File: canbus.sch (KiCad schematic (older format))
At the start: 17 parts, among them J1 Conn_01x08, J2 RJ45, J3 RJ45, U1 MCP2515-E/SO, U2 MCP2562-H/SN, Y1 Crystal_GND24

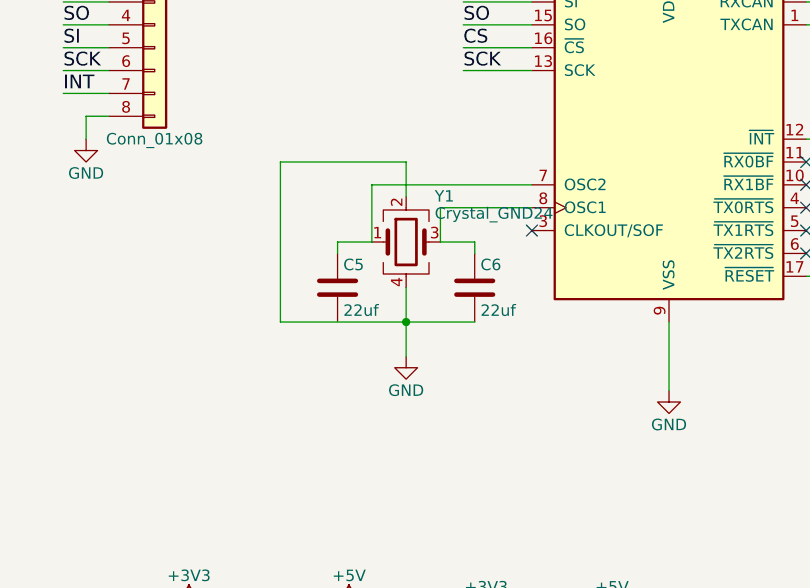
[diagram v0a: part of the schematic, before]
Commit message: Modified layout to include capacitors for oscillator
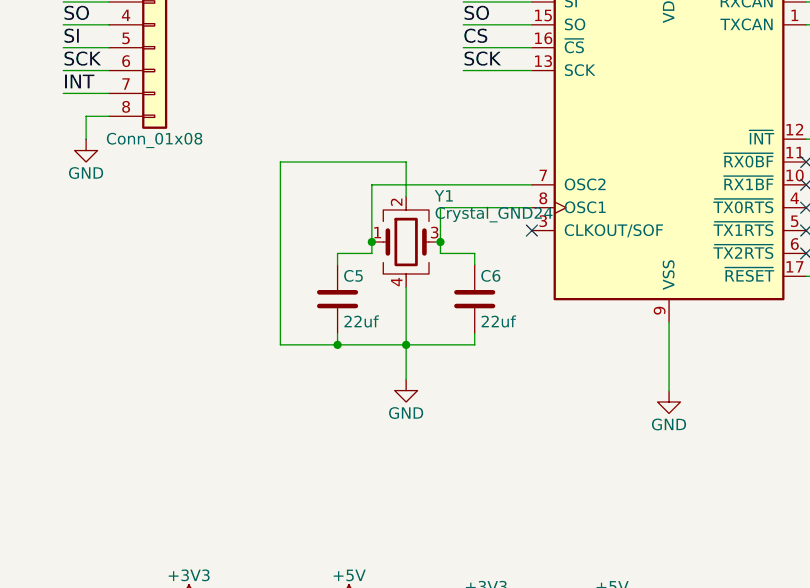
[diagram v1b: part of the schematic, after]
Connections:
- net GND: now also C5.2
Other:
- moved on the sheet: C5, C6
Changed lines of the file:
@@
 L GND #PWR05
 U 1 1 59E47374
-P 3300 4100
-F 0 "#PWR05" H 3300 3850 50  0001 C CNN
-F 1 "GND" H 3300 3950 50  0000 C CNN
-F 2 "" H 3300 4100 50  0001 C CNN
-F 3 "" H 3300 4100 50  0001 C CNN
-	1    3300 4100
+P 3300 4200
+F 0 "#PWR05" H 3300 3950 50  0001 C CNN
+F 1 "GND" H 3300 4050 50  0000 C CNN
+F 2 "" H 3300 4200 50  0001 C CNN
+F 3 "" H 3300 4200 50  0001 C CNN
+	1    3300 4200
 	1    0    0    -1
 $EndComp
@@
 	6200 2300 6200 2600
 Wire Wire Line
-	3450 3600 3450 3450
+	3450 3450 3450 3650
 Wire Wire Line
 	3450 3450 3850 3450
 Wire Wire Line
-	3150 3600 3150 3350
-Wire Wire Line
-	3150 3350 3850 3350
-Wire Wire Line
-	3300 3800 3300 4100
+	3150 3350 3150 3650
+Wire Wire Line
+	3300 3800 3300 4200
 Wire Wire Line
 	5050 3750 5150 3750
@@
 	3300 3250 2750 3250
 Wire Wire Line
-	2750 3250 2750 3950
-Wire Wire Line
-	2750 3950 3600 3950
-Connection ~ 3300 3950
+	2750 3250 2750 4050
+Wire Wire Line
+	2750 4050 3600 4050
+Connection ~ 3300 4050
 Wire Wire Line
 	8900 1950 8900 2000
@@
 L C C5
 U 1 1 5B05E18A
-P 3000 3800
-F 0 "C5" H 3025 3900 50  0000 L CNN
-F 1 "22uf" H 3025 3700 50  0000 L CNN
-F 2 "Capacitors_SMD:C_0805_HandSoldering" H 3038 3650 50  0001 C CNN
-F 3 "" H 3000 3800 50  0001 C CNN
-	1    3000 3800
+P 3000 3850
+F 0 "C5" H 3025 3950 50  0000 L CNN
+F 1 "22uf" H 3025 3750 50  0000 L CNN
+F 2 "Capacitors_SMD:C_0805_HandSoldering" H 3038 3700 50  0001 C CNN
+F 3 "" H 3000 3850 50  0001 C CNN
+	1    3000 3850
 	1    0    0    -1
 $EndComp
@@
 L C C6
 U 1 1 5B05E20B
-P 3600 3800
-F 0 "C6" H 3625 3900 50  0000 L CNN
-F 1 "22uf" H 3625 3700 50  0000 L CNN
-F 2 "Capacitors_SMD:C_0805_HandSoldering" H 3638 3650 50  0001 C CNN
-F 3 "" H 3600 3800 50  0001 C CNN
-	1    3600 3800
-	1    0    0    -1
-$EndComp
-Wire Wire Line
-	3000 3650 3000 3600
-Wire Wire Line
-	3000 3600 3150 3600
-Wire Wire Line
-	3450 3600 3600 3600
-Wire Wire Line
-	3600 3600 3600 3650
+P 3600 3850
+F 0 "C6" H 3625 3950 50  0000 L CNN
+F 1 "22uf" H 3625 3750 50  0000 L CNN
+F 2 "Capacitors_SMD:C_0805_HandSoldering" H 3638 3700 50  0001 C CNN
+F 3 "" H 3600 3850 50  0001 C CNN
+	1    3600 3850
+	1    0    0    -1
+$EndComp
+Wire Wire Line
+	3000 4000 3000 4050
+Connection ~ 3000 4050
+Wire Wire Line
+	3600 4050 3600 4000
+Wire Wire Line
+	3150 3350 3850 3350
+Wire Wire Line
+	3000 3700 3000 3650
+Wire Wire Line
+	3000 3650 3150 3650
+Connection ~ 3150 3600
+Wire Wire Line
+	3450 3650 3600 3650
+Wire Wire Line
+	3600 3650 3600 3700
+Connection ~ 3450 3600
 $EndSCHEMATC

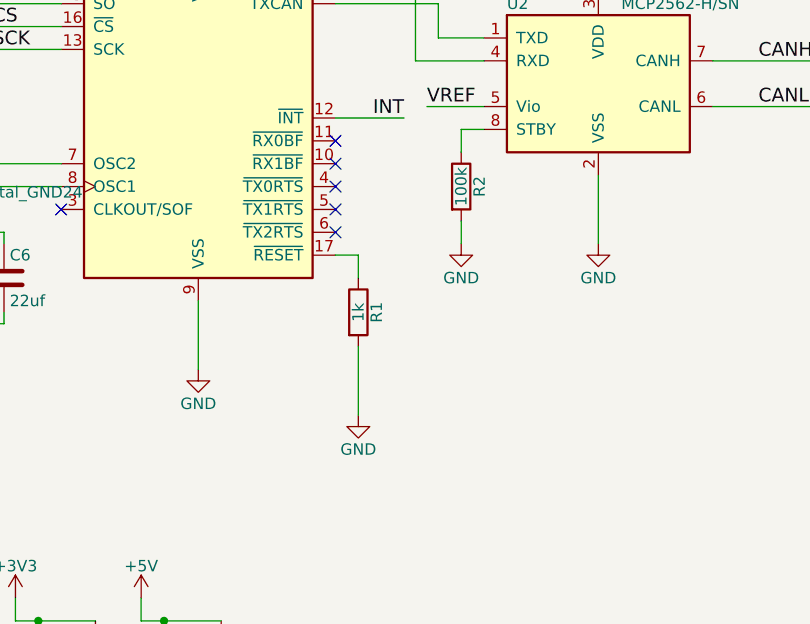
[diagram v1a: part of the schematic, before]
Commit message: Fixed MCP2515 Reset pullup
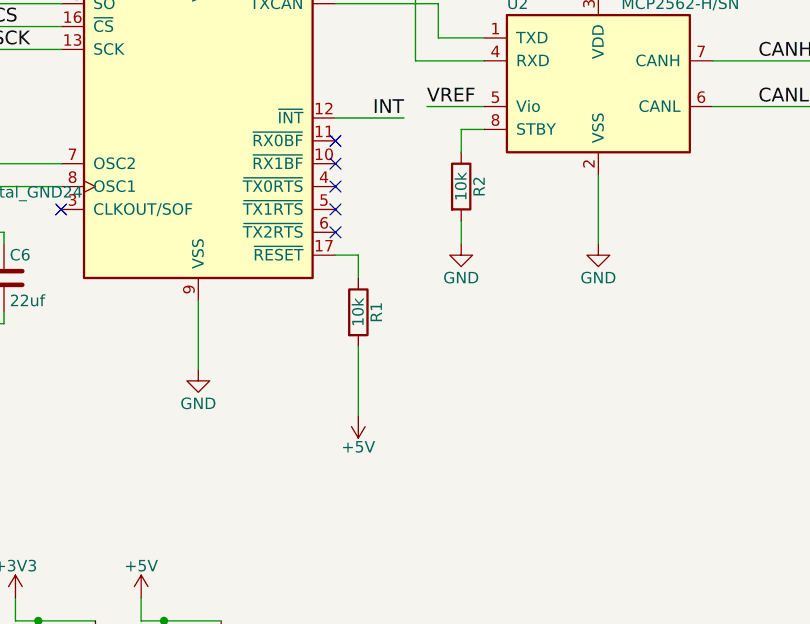
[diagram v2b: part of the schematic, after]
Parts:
- R1: value 1k -> 10k
- R2: value 100k -> 10k
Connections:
- net +5V: now also R1.2
- net GND: no longer R1.2
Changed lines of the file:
@@
 P 5600 3450
 F 0 "R2" V 5680 3450 50  0000 C CNN
-F 1 "100k" V 5600 3450 50  0000 C CNN
+F 1 "10k" V 5600 3450 50  0000 C CNN
 F 2 "Resistors_SMD:R_0805_HandSoldering" V 5530 3450 50  0001 C CNN
 F 3 "" H 5600 3450 50  0001 C CNN
@@
 P 5150 4000
 F 0 "R1" V 5230 4000 50  0000 C CNN
-F 1 "1k" V 5150 4000 50  0000 C CNN
+F 1 "10k" V 5150 4000 50  0000 C CNN
 F 2 "Resistors_SMD:R_0805_HandSoldering" V 5080 4000 50  0001 C CNN
 F 3 "" H 5150 4000 50  0001 C CNN
 	1    5150 4000
-	1    0    0    -1
-$EndComp
-$Comp
-L GND #PWR06
-U 1 1 59E4A43B
-P 5150 4450
-F 0 "#PWR06" H 5150 4200 50  0001 C CNN
-F 1 "GND" H 5150 4300 50  0000 C CNN
-F 2 "" H 5150 4450 50  0001 C CNN
-F 3 "" H 5150 4450 50  0001 C CNN
-	1    5150 4450
 	1    0    0    -1
 $EndComp
@@
 INT
 $Comp
-L +5V #PWR07
+L +5V #PWR06
 U 1 1 59E4D6B5
 P 1900 2250
-F 0 "#PWR07" H 1900 2100 50  0001 C CNN
+F 0 "#PWR06" H 1900 2100 50  0001 C CNN
 F 1 "+5V" H 1900 2390 50  0000 C CNN
 F 2 "" H 1900 2250 50  0001 C CNN
@@
 $EndComp
 $Comp
-L GND #PWR08
+L GND #PWR07
 U 1 1 59E4D6DB
 P 1900 3150
-F 0 "#PWR08" H 1900 2900 50  0001 C CNN
+F 0 "#PWR07" H 1900 2900 50  0001 C CNN
 F 1 "GND" H 1900 3000 50  0000 C CNN
 F 2 "" H 1900 3150 50  0001 C CNN
@@
 $EndComp
 $Comp
-L +5V #PWR09
+L +5V #PWR08
 U 1 1 59E4DFD1
 P 3050 5200
-F 0 "#PWR09" H 3050 5050 50  0001 C CNN
+F 0 "#PWR08" H 3050 5050 50  0001 C CNN
 F 1 "+5V" H 3050 5340 50  0000 C CNN
 F 2 "" H 3050 5200 50  0001 C CNN
@@
 $EndComp
 $Comp
-L +3V3 #PWR010
+L +3V3 #PWR09
 U 1 1 59E4DFF9
 P 2350 5200
-F 0 "#PWR010" H 2350 5050 50  0001 C CNN
+F 0 "#PWR09" H 2350 5050 50  0001 C CNN
 F 1 "+3V3" H 2350 5340 50  0000 C CNN
 F 2 "" H 2350 5200 50  0001 C CNN
@@
 VREF
 $Comp
-L +3V3 #PWR011
+L +3V3 #PWR010
 U 1 1 59E594BB
 P 1700 2350
-F 0 "#PWR011" H 1700 2200 50  0001 C CNN
+F 0 "#PWR010" H 1700 2200 50  0001 C CNN
 F 1 "+3V3" H 1700 2490 50  0000 C CNN
 F 2 "" H 1700 2350 50  0001 C CNN
@@
 $EndComp
 $Comp
-L GND #PWR012
+L GND #PWR011
 U 1 1 59E59D18
 P 3650 5750
-F 0 "#PWR012" H 3650 5500 50  0001 C CNN
+F 0 "#PWR011" H 3650 5500 50  0001 C CNN
 F 1 "GND" H 3650 5600 50  0000 C CNN
 F 2 "" H 3650 5750 50  0001 C CNN
@@
 $EndComp
 $Comp
-L +5V #PWR013
+L +5V #PWR012
 U 1 1 59E5A90B
 P 4200 5250
-F 0 "#PWR013" H 4200 5100 50  0001 C CNN
+F 0 "#PWR012" H 4200 5100 50  0001 C CNN
 F 1 "+5V" H 4200 5390 50  0000 C CNN
 F 2 "" H 4200 5250 50  0001 C CNN
@@
 $EndComp
 $Comp
-L +3V3 #PWR014
+L +3V3 #PWR013
 U 1 1 59E5A952
 P 3650 5250
-F 0 "#PWR014" H 3650 5100 50  0001 C CNN
+F 0 "#PWR013" H 3650 5100 50  0001 C CNN
 F 1 "+3V3" H 3650 5390 50  0000 C CNN
 F 2 "" H 3650 5250 50  0001 C CNN
@@
 $EndComp
 $Comp
-L GND #PWR015
+L GND #PWR014
 U 1 1 59E5AC7A
 P 4200 5750
-F 0 "#PWR015" H 4200 5500 50  0001 C CNN
+F 0 "#PWR014" H 4200 5500 50  0001 C CNN
 F 1 "GND" H 4200 5600 50  0000 C CNN
 F 2 "" H 4200 5750 50  0001 C CNN
@@
 Connection ~ 9600 2250
 $Comp
-L GND #PWR016
+L GND #PWR015
 U 1 1 59FCC298
 P 9600 2600
-F 0 "#PWR016" H 9600 2350 50  0001 C CNN
+F 0 "#PWR015" H 9600 2350 50  0001 C CNN
 F 1 "GND" H 9600 2450 50  0000 C CNN
 F 2 "" H 9600 2600 50  0001 C CNN
@@
 	3600 3650 3600 3700
 Connection ~ 3450 3600
+$Comp
+L +5V #PWR?
+U 1 1 5B085582
+P 5150 4450
+F 0 "#PWR?" H 5150 4300 50  0001 C CNN
+F 1 "+5V" H 5150 4590 50  0000 C CNN
+F 2 "" H 5150 4450 50  0001 C CNN
+F 3 "" H 5150 4450 50  0001 C CNN
+	1    5150 4450
+	-1   0    0    1
+$EndComp
 $EndSCHEMATC
